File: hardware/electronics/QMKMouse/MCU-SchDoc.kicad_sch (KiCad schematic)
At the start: 14 parts

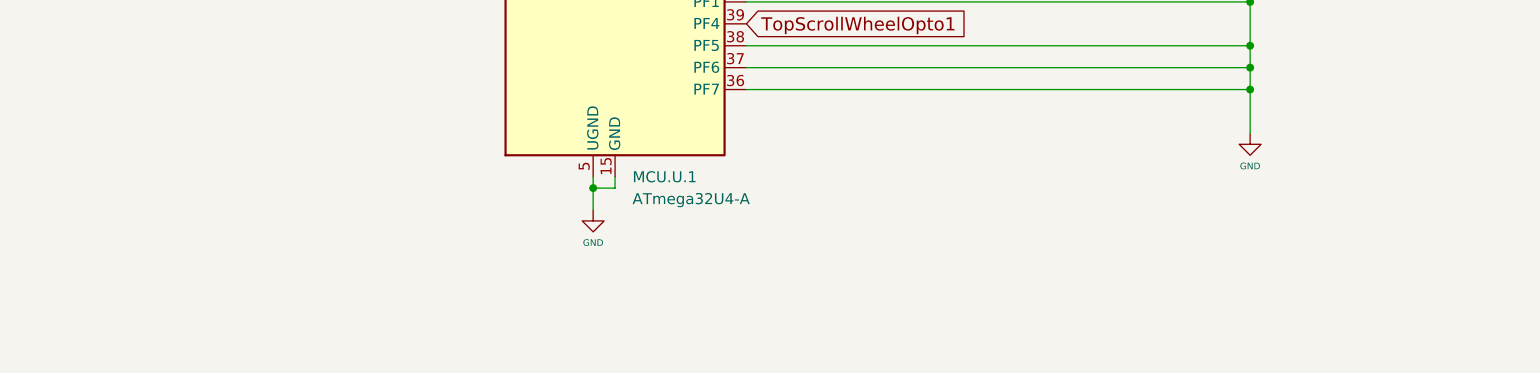
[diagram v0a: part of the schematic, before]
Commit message: update schematic components
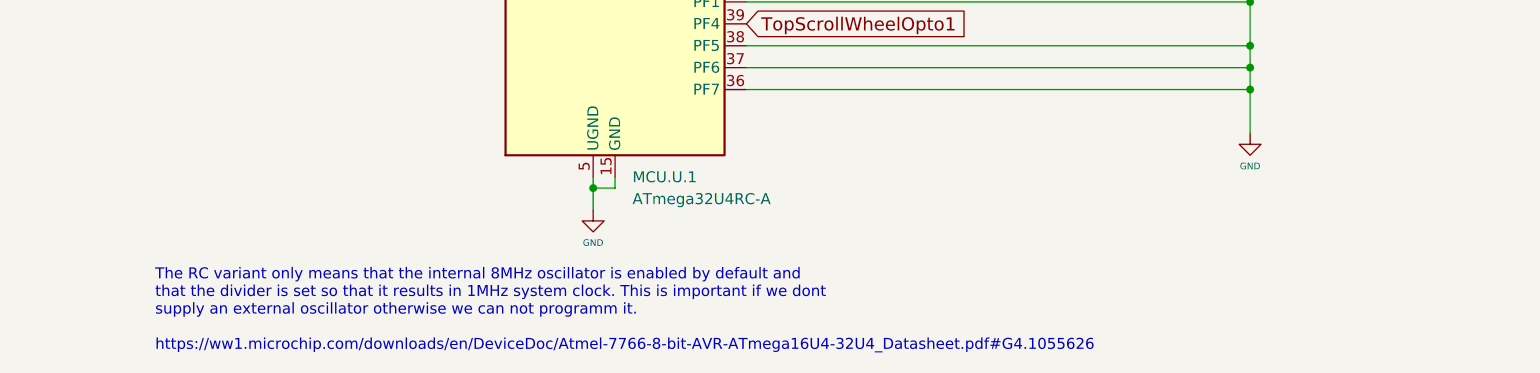
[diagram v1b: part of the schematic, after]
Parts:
- MCU.U.1: value ATmega32U4-A -> ATmega32U4RC-A
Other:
- note added: "The RC variant only means that the internal 8MHz oscillator is enabled by default and that the divider is set so that it results in 1MHz system clock. This is important if we dont supply an external oscillator otherwise we can not programm it. https://ww1.microchip.com/downloads/en/DeviceDoc/Atmel-7766-8-bit-AVR-ATmega16U4-32U4_Datasheet.pdf#G4.1055626"
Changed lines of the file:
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@@
     (stroke (width 0) (type default) (color 0 0 0 0))
+  )
+  (text "The RC variant only means that the internal 8MHz oscillator is enabled by default and \nthat the divider is set so that it results in 1MHz system clock. This is important if we dont \nsupply an external oscillator otherwise we can not programm it.\n\nhttps://ww1.microchip.com/downloads/en/DeviceDoc/Atmel-7766-8-bit-AVR-ATmega16U4-32U4_Datasheet.pdf#G4.1055626"
+    (at 52.07 171.45 0)
+    (effects (font (size 1.27 1.27)) (justify left bottom))
   )
   (text "IMPORTANT NOTE:\n\nUnused GPIO are grounded to \nimprove EMC performance. To \nmake best use of this, grounded \nGPIO should be set to:    \n\nOUTPUT LOW + PULLDOWN    \n\nThis will ground the chip through\nthe GPIO pins."
@@
       (effects (font (size 1.27 1.27)) (justify left))
     )
-    (property "Value" "ATmega32U4-A" (id 1) (at 107.4294 153.67 0)
-      (effects (font (size 1.27 1.27)) (justify left))
-    )
+    (property "Value" "ATmega32U4RC-A" (id 1) (at 107.4294 153.67 0)
+      (effects (font (size 1.27 1.27)) (justify left))
+    )

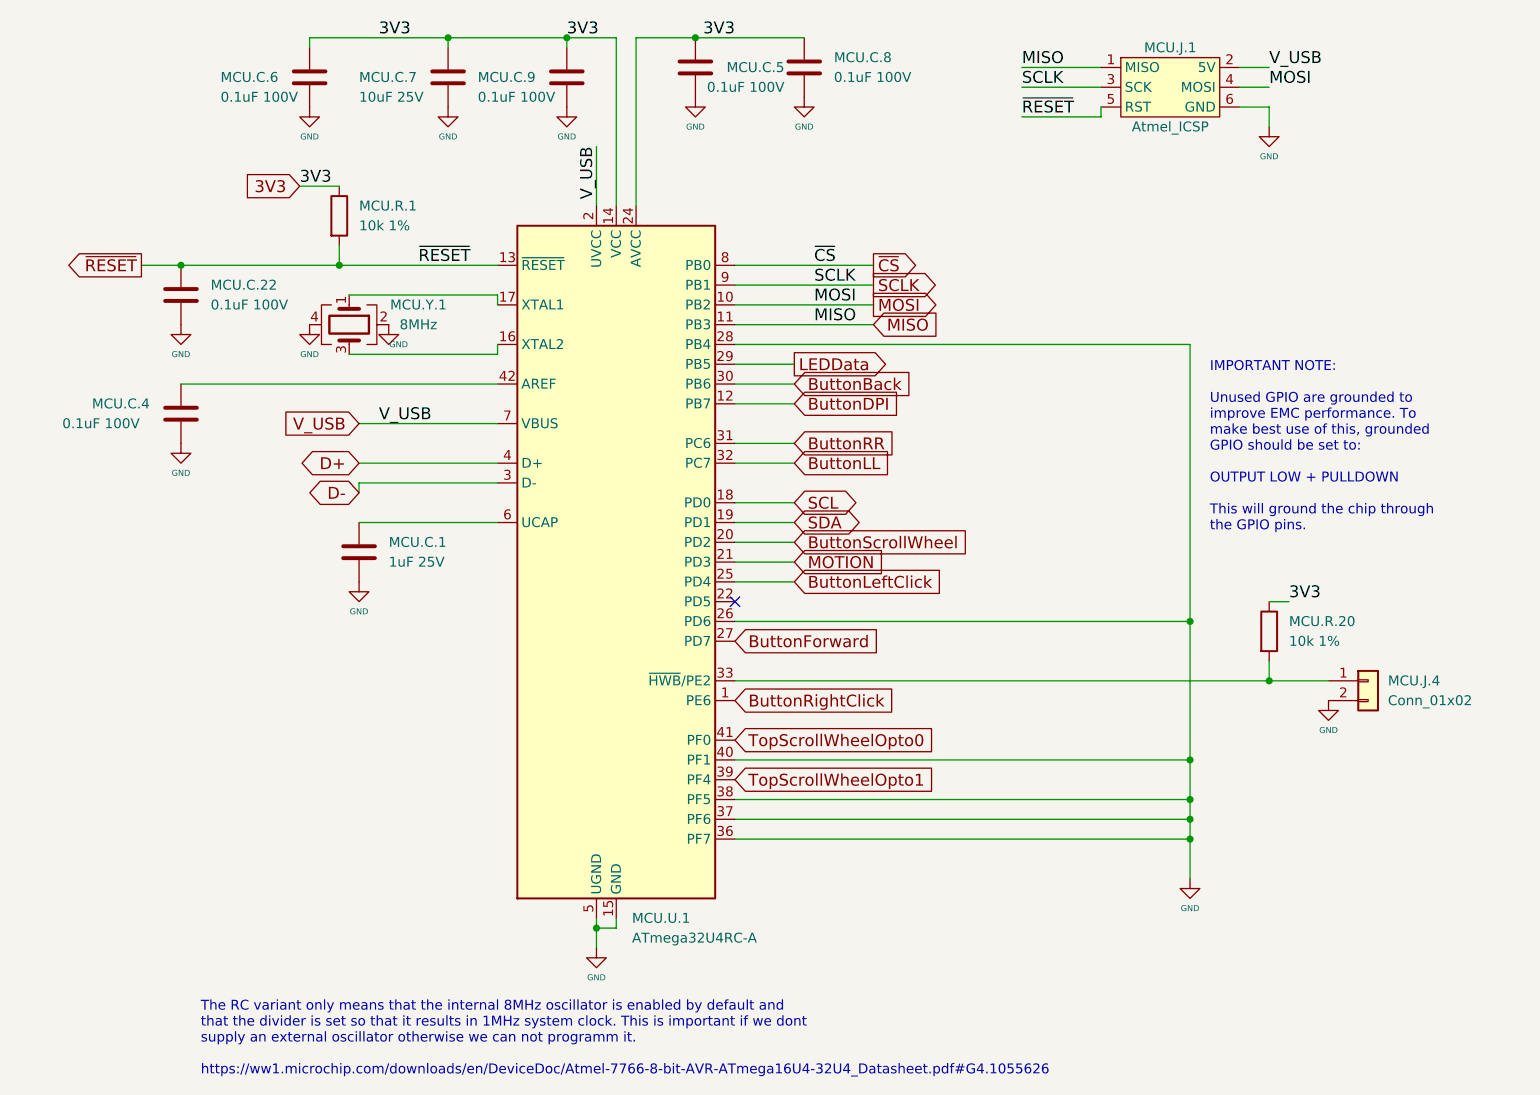
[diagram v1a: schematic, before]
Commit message: update schematic from PCB; sync netlist and fix some symbol orientations; also fix LED symbol
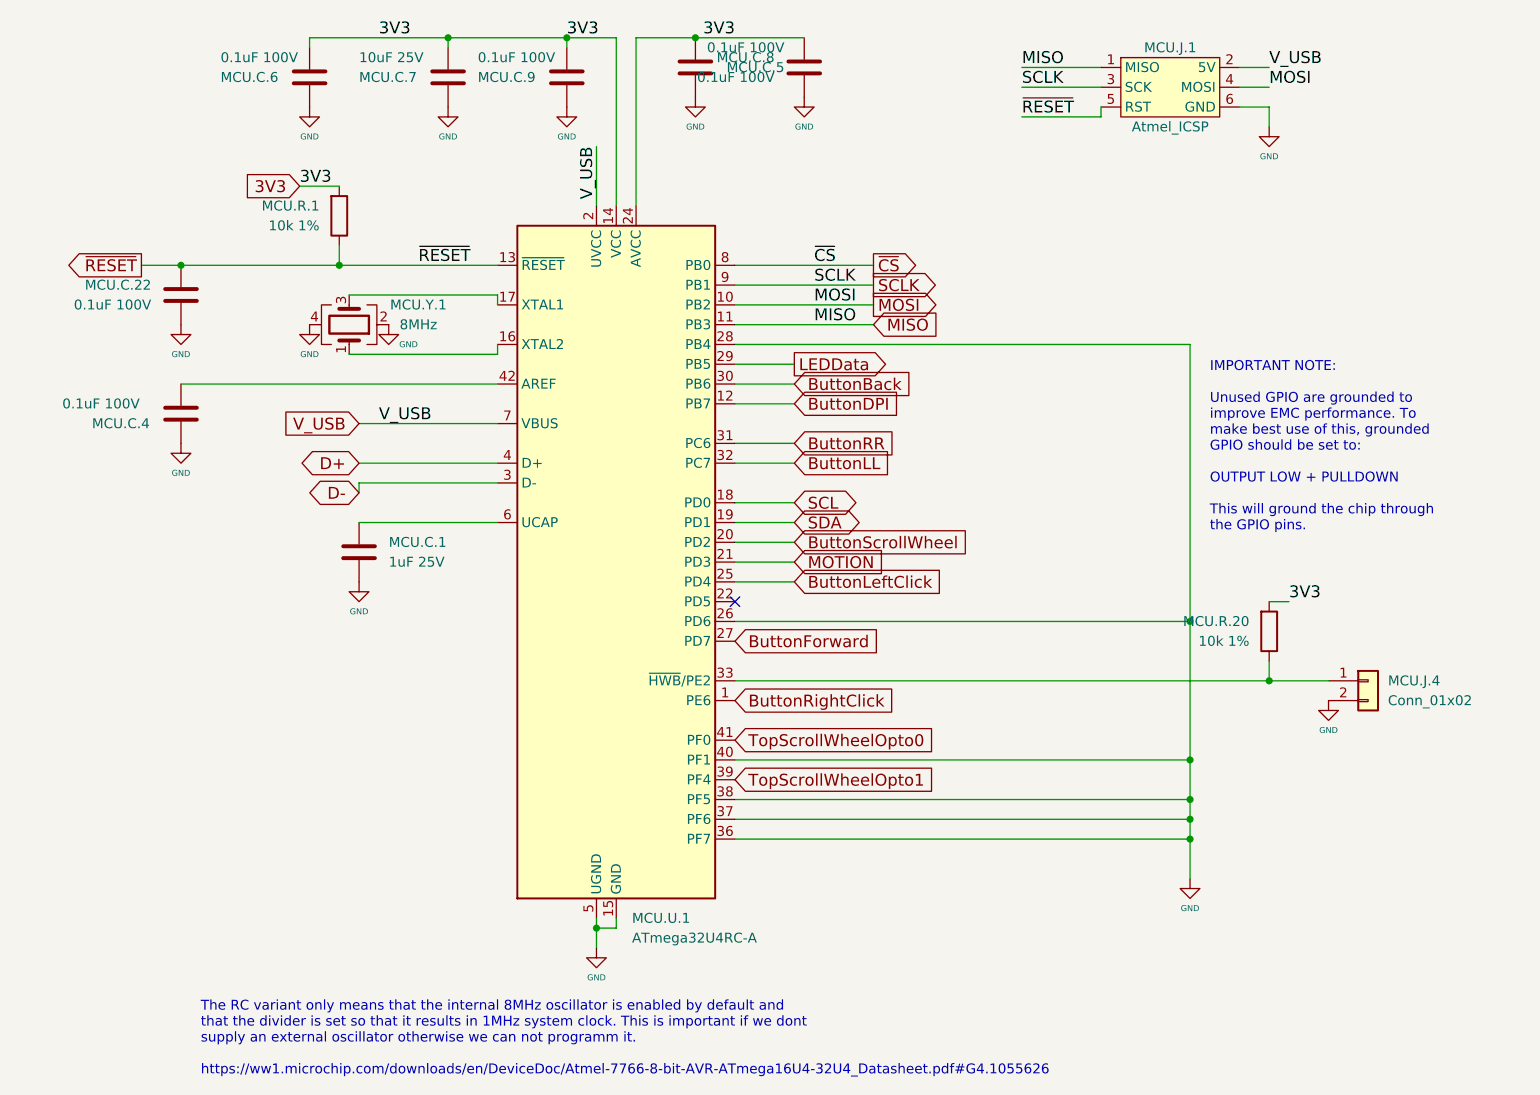
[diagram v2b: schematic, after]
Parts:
- MCU.C.1, MCU.C.22, MCU.C.4, MCU.C.5, MCU.C.6, MCU.C.7, MCU.C.8, MCU.C.9: footprint Capacitor_SMD:C_0805_2012Metric -> Chip_Passives.PcbLib:0805
- MCU.J.1: footprint Connector_PinHeader_1.00mm:PinHeader_2x03_P1.00mm_Vertical -> Connectors.PcbLib:6x2
- MCU.J.4: footprint Connector_PinHeader_1.00mm:PinHeader_1x02_P1.00mm_Vertical -> Connectors.PcbLib:2x1
- MCU.R.1, MCU.R.20: footprint Resistor_SMD:R_0805_2012Metric -> Chip_Passives.PcbLib:0805
- MCU.U.1: footprint Package_QFP:TQFP-44_10x10mm_P0.8mm -> MCUs.PcbLib:ATMEGA32U4 - TQFP80P1200X1200X120-44N
- MCU.Y.1: footprint Crystal:Crystal_SMD_5032-4Pin_5.0x3.2mm -> Crystals.PcbLib:LFXTAL055663BULK
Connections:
- net 3V3: now also MCU.C.5.2, MCU.C.6.2, MCU.C.7.2, MCU.C.8.2, MCU.C.9.2, MCU.R.1.2, MCU.R.20.2; no longer MCU.C.5.1, MCU.C.6.1, MCU.C.7.1, MCU.C.8.1, MCU.C.9.1, MCU.R.1.1, MCU.R.20.1
- net GND: now also MCU.C.22.1, MCU.C.4.1, MCU.C.5.1, MCU.C.6.1, MCU.C.7.1, MCU.C.8.1, MCU.C.9.1; no longer MCU.C.22.2, MCU.C.4.2, MCU.C.5.2, MCU.C.6.2, MCU.C.7.2, MCU.C.8.2, MCU.C.9.2
- net ~{RESET}: now also MCU.C.22.2, MCU.R.1.1; no longer MCU.C.22.1, MCU.R.1.2
- net at MCU.Y.1.1: now also MCU.U.1.16 (XTAL2); no longer MCU.U.1.17 (XTAL1)
- net at MCU.Y.1.3: now also MCU.U.1.17 (XTAL1); no longer MCU.U.1.16 (XTAL2)
- net at MCU.U.1.42 (AREF): now also MCU.C.4.2; no longer MCU.C.4.1
- net at MCU.J.4.1 (Pin_1), MCU.U.1.33 (~{HWB}/PE2): now also MCU.R.20.1; no longer MCU.R.20.2
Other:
- moved on the sheet: MCU.C.5

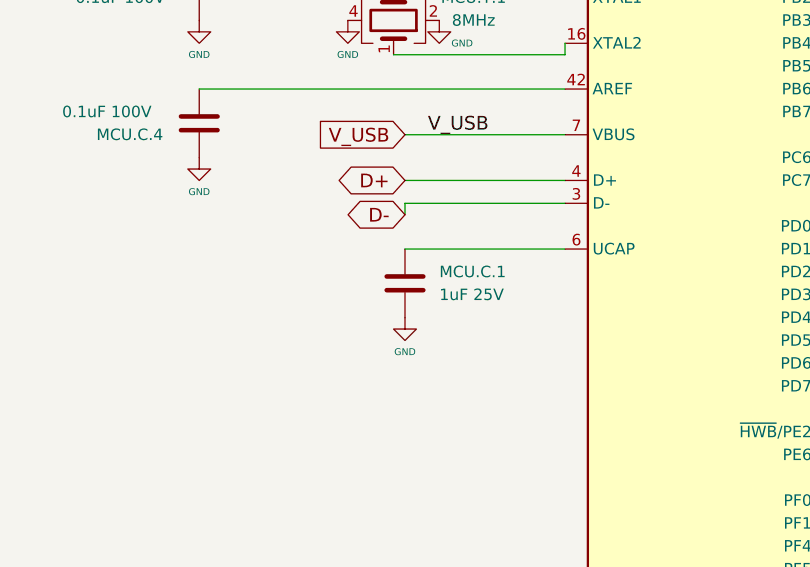
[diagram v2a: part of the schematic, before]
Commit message: Fix some schematic PCB mismatch
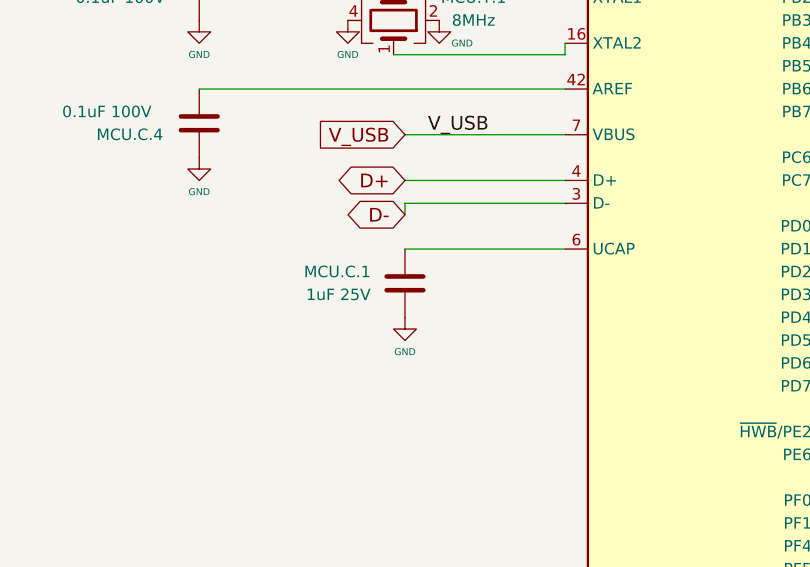
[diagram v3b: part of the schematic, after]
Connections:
- net GND: now also MCU.C.1.1; no longer MCU.C.1.2
- net at MCU.U.1.6 (UCAP): now also MCU.C.1.2; no longer MCU.C.1.1
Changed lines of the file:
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@@
     (pin "2")
   )
-  (symbol (lib_id "Device:C") (at 72.39 104.14 0) (unit 1)
+  (symbol (lib_id "Device:C") (at 72.39 104.14 0) (mirror x) (unit 1)
     (in_bom yes) (on_board yes) (fields_autoplaced)
-    (property "Reference" "MCU.C.1" (id 0) (at 76.2 102.8699 0)
-      (effects (font (size 1.27 1.27)) (justify left))
+    (property "Reference" "MCU.C.1" (id 0) (at 68.58 102.8699 0)
+      (effects (font (size 1.27 1.27)) (justify right))
     )
-    (property "Value" "1uF 25V" (id 1) (at 76.2 105.4099 0)
-      (effects (font (size 1.27 1.27)) (justify left))
+    (property "Value" "1uF 25V" (id 1) (at 68.58 105.4099 0)
+      (effects (font (size 1.27 1.27)) (justify right))
     )
-    (property "Footprint" "Chip_Passives.PcbLib:0805" (id 2) (at 73.3552 107.95 0)
+    (property "Footprint" "Chip_Passives.PcbLib:0805" (id 2) (at 73.3552 100.33 0)
       (effects (font (size 1.27 1.27)) hide)
     )
